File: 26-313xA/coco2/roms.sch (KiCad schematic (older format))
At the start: 8 parts, among them IC8 27C128, J1 128K 64K, J2 64K 128K, J3 128K 64K, J4 128K 64K, J5 128K 64K

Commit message: -Corrected some part numbers in the BOM -Updated paret numbers for some parts in the schematic.
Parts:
- C4: Manufacturer part# FG28C0G1H103JNT06 -> RDER71H104K0K1H03B; Vendor part# 445-173474-1-ND -> 490-8814-ND
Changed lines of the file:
@@
 F 1 ".1uF" V 7650 2450 50  0000 C CNN
 F 2 "Capacitor_THT:C_Disc_D4.7mm_W2.5mm_P5.00mm" H 7800 2450 50  0001 C CNN
-F 3 " https://product.tdk.com/info/en/catalog/datasheets/leadmlcc_halogenfree_fg_en.pdf?ref_disty=digikey" H 7800 2450 50  0001 C CNN
+F 3 " https://search.murata.co.jp/Ceramy/image/img/A01X/G101/ENG/RDE_X7R_250V-1kV_E.pdf" H 7800 2450 50  0001 C CNN
 F 4 "digikey" V 7800 2450 50  0001 C CNN "Vendor"
-F 5 "445-173474-1-ND" V 7800 2450 50  0001 C CNN "Vendor part#"
-F 6 "FG28C0G1H103JNT06" H 7800 2450 50  0001 C CNN "Manufacturer part#"
+F 5 "490-8814-ND" V 7800 2450 50  0001 C CNN "Vendor part#"
+F 6 "RDER71H104K0K1H03B" H 7800 2450 50  0001 C CNN "Manufacturer part#"
 	1    7800 2450
 	0    -1   -1   0

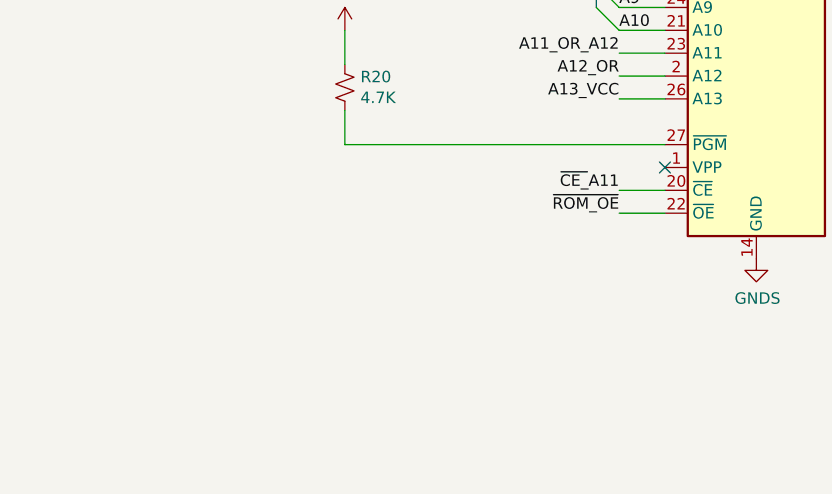
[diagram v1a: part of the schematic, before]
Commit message: -moved power switch 4mm into the board. -moved reset switch 1mm towards the DIN connectors. -moved channel select switch .5mm into the DIN connectors. -shortened length of board from cart to power connector 1mm. -updated image,layout,schematic and BOM's
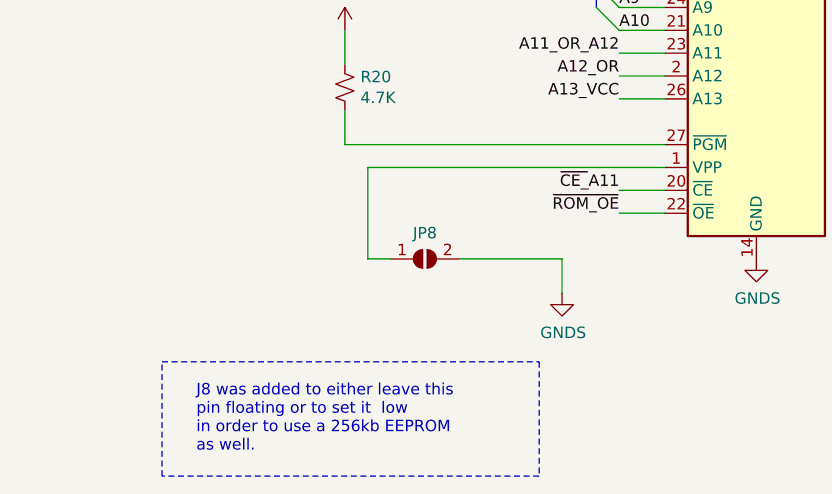
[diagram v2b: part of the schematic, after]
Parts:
- added JP8: SolderJumper_2_Open, Jumper:SolderJumper-2_P1.3mm_Open_RoundedPad1.0x1.5mm, symbol Jumper:SolderJumper_2_Open
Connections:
- net GNDS: now also JP8.2 (B)
- net at IC8.1 (VPP): now also JP8.1 (A)
- no-connect marks 1 -> 0
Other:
- note added: "J8 was added to either leave this\npin floating or to set it low\nin order to use a 256kb EEPROM\nas well."
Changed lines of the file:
@@
 Wire Bus Line
 	6300 1650 6550 1650
-NoConn ~ 6850 4600
 Entry Wire Line
 	6650 2250 6550 2150
@@
 Text HLabel 2200 4700 0    50   Input ~ 0
 128K_ROM_~CE
+Wire Wire Line
+	6850 4600 5550 4600
+$Comp
+L power:GNDS #PWR?
+U 1 1 62EFE478
+P 6400 5150
+AR Path="/602A51A8/62EFE478" Ref="#PWR?"  Part="1"
+AR Path="/60308A73/62EFE478" Ref="#PWR03"  Part="1"
+F 0 "#PWR03" H 6400 4900 50  0001 C CNN
+F 1 "GNDS" H 6405 4977 50  0000 C CNN
+F 2 "" H 6400 5150 50  0001 C CNN
+F 3 "" H 6400 5150 50  0001 C CNN
+	1    6400 5150
+	1    0    0    -1
+$EndComp
+Wire Wire Line
+	6400 5000 6400 5150
+Text Notes 4800 5850 0    50   ~ 0
+J8 was added to either leave this\npin floating or to set it  low\nin order to use a 256kb EEPROM\nas well.
+Wire Notes Line
+	4650 5450 6300 5450
+Wire Notes Line
+	6300 5450 6300 5950
+Wire Notes Line
+	6300 5950 4650 5950
+Wire Notes Line
+	4650 5950 4650 5450
+$Comp
+L Jumper:SolderJumper_2_Open JP8
+U 1 1 62F1741F
+P 5800 5000
+F 0 "JP8" H 5800 5113 50  0000 C CNN
+F 1 "SolderJumper_2_Open" H 5800 5114 50  0001 C CNN
+F 2 "Jumper:SolderJumper-2_P1.3mm_Open_RoundedPad1.0x1.5mm" H 5800 5000 50  0001 C CNN
+F 3 "~" H 5800 5000 50  0001 C CNN
+	1    5800 5000
+	1    0    0    -1
+$EndComp
+Wire Wire Line
+	5950 5000 6400 5000
+Wire Wire Line
+	5550 5000 5650 5000
+Wire Wire Line
+	5550 4600 5550 5000
 Wire Bus Line
 	8050 3100 8050 5400
